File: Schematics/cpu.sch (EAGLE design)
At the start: 42 parts, among them IC10 74LS32N, IC2 LM555N, IC3 LM555N, IC4 7400N, IC5 74LS32N, IC6 74LS32N, IC7 74LS32N, IC8 74154N, IC9 74154N, U1 74HC245N,652, U10 74HC373N,652, U11 74HC373N,652, U12 74HC373N,652, U13 74HC373N,652, U14 74HC373N,652, U15 74HC373N,652, U2 74HC245N,652, U3 74HC245N,652, U4 74HC04N,652, U5 74HC373N,652, U6 74HC373N,652, U7 74HC373N,652, U8 74HC373N,652, U9 74HC373N,652

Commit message: started on video board
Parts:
- added U$5: DB15, SparkFun-Connectors:DB15
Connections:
- new net BLUE: U$5.3
- new net GREEN: U$5.2
- new net HSYNC: U$5.13
- new net RED: U$5.1
- new net VSYNC: U$5.14
- net GND: now also U$5.10, U$5.5, U$5.6, U$5.7, U$5.8, U$5.9
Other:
- note added: "Note: Medium speed SRAM is needed 25MHz => 40ns 12.5MHz => 80ns IDT71256SA AS6C62256 SST39SF040"
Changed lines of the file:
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@@
 <part name="GND26" library="SparkFun-Aesthetics" deviceset="GND" device=""/>
 <part name="SUPPLY11" library="SparkFun-Aesthetics" deviceset="VCC" device="" value="+5V"/>
+<part name="U$5" library="SparkFun-Connectors" deviceset="DB15" device=""/>
+<part name="GND27" library="supply1" deviceset="GND" device=""/>
 </parts>
 <sheets>
@@
 </segment>
 </net>
+</nets>
+</sheet>
+<sheet>
+<description>VGA Video Generator</description>
+<plain>
+<text x="10.16" y="30.48" size="1.778" layer="97">Note:
+Medium speed SRAM is needed
+25MHz =&gt; 40ns
+12.5MHz =&gt; 80ns
+IDT71256SA
+AS6C62256
+SST39SF040</text>
+</plain>
+<instances>
+<instance part="U$5" gate="G$1" x="53.34" y="-2.54"/>
+<instance part="GND27" gate="1" x="40.64" y="-30.48"/>
+</instances>
+<busses>
+</busses>
+<nets>
+<net name="RED" class="0">
+<segment>
+<pinref part="U$5" gate="G$1" pin="1"/>
+<wire x1="45.72" y1="5.08" x2="33.02" y2="5.08" width="0.1524" layer="91"/>
+<label x="35.56" y="5.08" size="1.778" layer="95"/>
+</segment>
+</net>
+<net name="GREEN" class="0">
+<segment>
+<pinref part="U$5" gate="G$1" pin="2"/>
+<wire x1="45.72" y1="0" x2="33.02" y2="0" width="0.1524" layer="91"/>
+<label x="35.56" y="0" size="1.778" layer="95"/>
+</segment>
+</net>
+<net name="BLUE" class="0">
+<segment>
+<pinref part="U$5" gate="G$1" pin="3"/>
+<wire x1="45.72" y1="-5.08" x2="33.02" y2="-5.08" width="0.1524" layer="91"/>
+<label x="35.56" y="-5.08" size="1.778" layer="95"/>
+</segment>
+</net>
+<net name="HSYNC" class="0">
+<segment>
+<pinref part="U$5" gate="G$1" pin="13"/>
+<wire x1="61.214" y1="-5.08" x2="73.66" y2="-5.08" width="0.1524" layer="91"/>
+<label x="68.58" y="-5.08" size="1.778" layer="95"/>
+</segment>
+</net>
+<net name="VSYNC" class="0">
+<segment>
+<pinref part="U$5" gate="G$1" pin="14"/>
+<wire x1="61.214" y1="-10.16" x2="73.66" y2="-10.16" width="0.1524" layer="91"/>
+<label x="68.58" y="-10.16" size="1.778" layer="95"/>
+</segment>
+</net>
+<net name="GND" class="0">
+<segment>
+<pinref part="U$5" gate="G$1" pin="6"/>
+<wire x1="61.214" y1="7.62" x2="63.5" y2="7.62" width="0.1524" layer="91"/>
+<wire x1="63.5" y1="7.62" x2="63.5" y2="2.54" width="0.1524" layer="91"/>
+<wire x1="63.5" y1="2.54" x2="63.5" y2="-2.54" width="0.1524" layer="91"/>
+<wire x1="63.5" y1="-2.54" x2="63.5" y2="-7.62" width="0.1524" layer="91"/>
+<wire x1="63.5" y1="-7.62" x2="63.5" y2="-12.7" width="0.1524" layer="91"/>
+<pinref part="U$5" gate="G$1" pin="10"/>
+<wire x1="61.214" y1="-12.7" x2="63.5" y2="-12.7" width="0.1524" layer="91"/>
+<junction x="63.5" y="-12.7"/>
+<pinref part="U$5" gate="G$1" pin="9"/>
+<wire x1="61.214" y1="-7.62" x2="63.5" y2="-7.62" width="0.1524" layer="91"/>
+<junction x="63.5" y="-7.62"/>
+<pinref part="U$5" gate="G$1" pin="8"/>
+<wire x1="61.214" y1="-2.54" x2="63.5" y2="-2.54" width="0.1524" layer="91"/>
+<junction x="63.5" y="-2.54"/>
+<pinref part="U$5" gate="G$1" pin="7"/>
+<wire x1="61.214" y1="2.54" x2="63.5" y2="2.54" width="0.1524" layer="91"/>
+<junction x="63.5" y="2.54"/>
+<wire x1="63.5" y1="-12.7" x2="63.5" y2="-22.86" width="0.1524" layer="91"/>
+<pinref part="U$5" gate="G$1" pin="5"/>
+<wire x1="45.72" y1="-15.24" x2="40.64" y2="-15.24" width="0.1524" layer="91"/>
+<wire x1="40.64" y1="-15.24" x2="40.64" y2="-22.86" width="0.1524" layer="91"/>
+<wire x1="63.5" y1="-22.86" x2="40.64" y2="-22.86" width="0.1524" layer="91"/>
+<wire x1="40.64" y1="-22.86" x2="40.64" y2="-27.94" width="0.1524" layer="91"/>
+<junction x="40.64" y="-22.86"/>
+<pinref part="GND27" gate="1" pin="GND"/>
+</segment>
+</net>

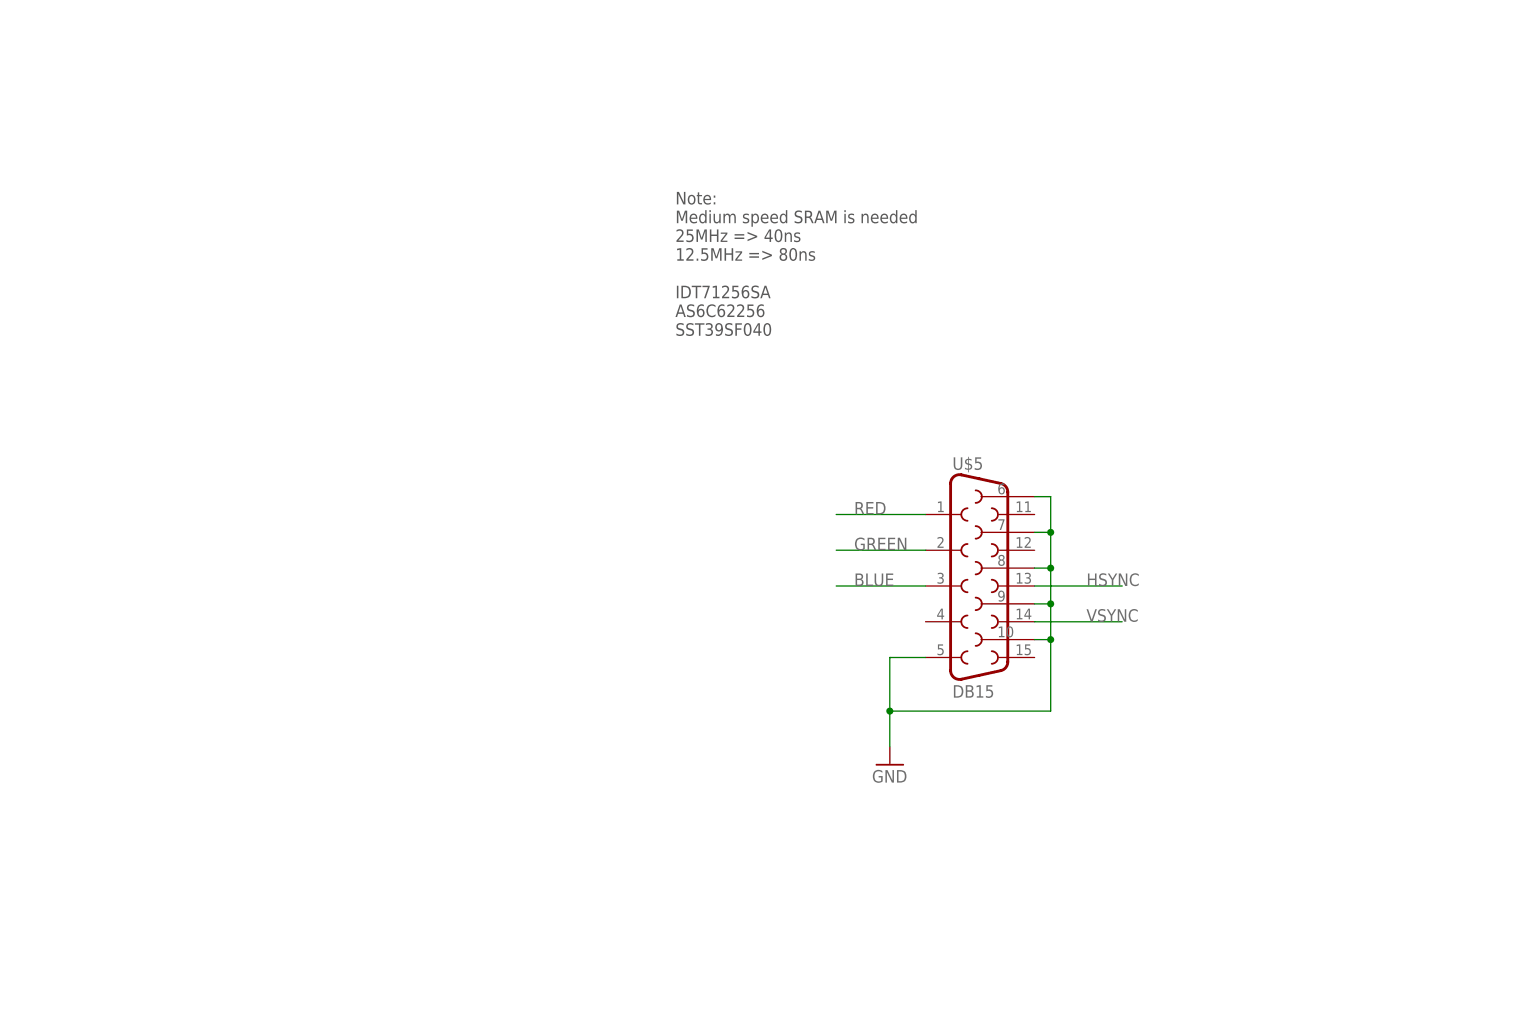
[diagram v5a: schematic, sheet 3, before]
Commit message: created resistor ladder
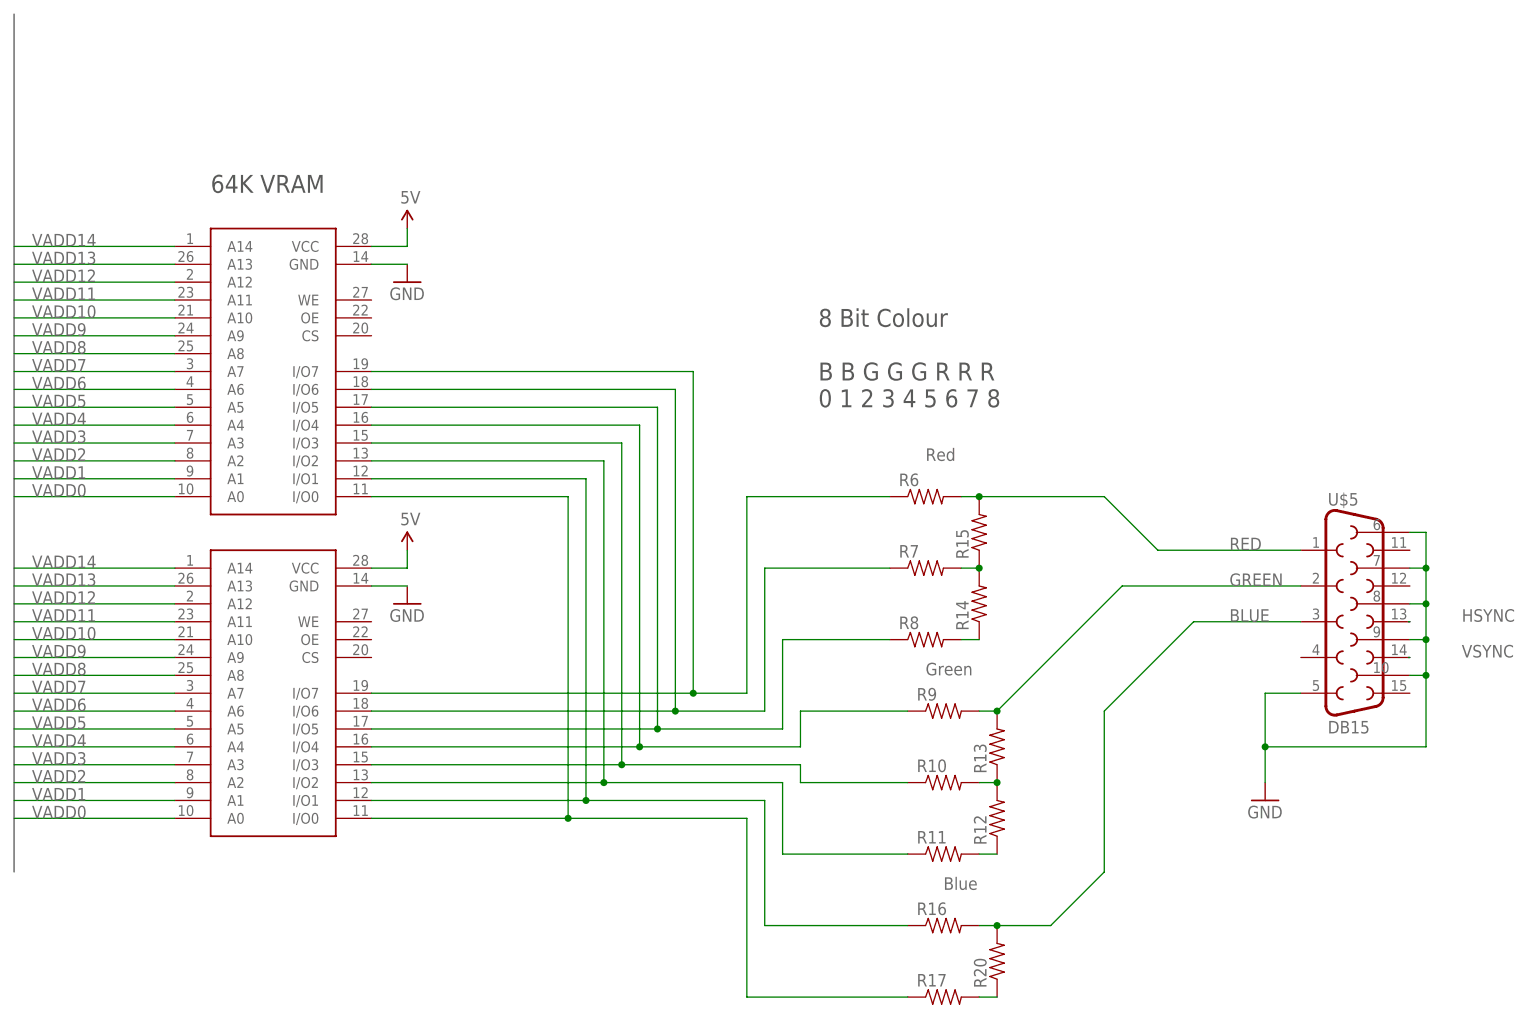
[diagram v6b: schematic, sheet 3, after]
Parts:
- added R10, R11, R12, R13, R14, R15, R16, R17, R20, R6, R7, R8, R9: (no value), SparkFun-Resistors:RESISTORPTH-1/4W
- added U$6, U$7: IDT71256SA, JacobBooth:IDT71256SA
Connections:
- new net N$41: R17.1, U$6.I/O0, U$7.I/O0
- new net N$42: R16.1, U$6.I/O1, U$7.I/O1
- new net N$43: R11.1, U$6.I/O2, U$7.I/O2
- new net N$44: R10.1, U$6.I/O3, U$7.I/O3
- new net N$45: R9.1, U$6.I/O4, U$7.I/O4
- new net N$46: R8.1, U$6.I/O5, U$7.I/O5
- new net N$47: R7.1, U$6.I/O6, U$7.I/O6
- new net N$48: R6.1, U$6.I/O7, U$7.I/O7
- new net N$49: R14.1, R8.2
- new net N$52: R14.2, R15.1, R7.2
- new net N$56: R11.2, R12.1
- new net N$57: R10.2, R12.2, R13.1
- new net N$62: R17.2, R20.1
- new net VADD0: U$6.A0, U$7.A0
- new net VADD1: U$6.A1, U$7.A1
- new net VADD10: U$6.A10, U$7.A10
- new net VADD11: U$6.A11, U$7.A11
- new net VADD12: U$6.A12, U$7.A12
- new net VADD13: U$6.A13, U$7.A13
- new net VADD14: U$6.A14, U$7.A14
- new net VADD2: U$6.A2, U$7.A2
- new net VADD3: U$6.A3, U$7.A3
- new net VADD4: U$6.A4, U$7.A4
- new net VADD5: U$6.A5, U$7.A5
- new net VADD6: U$6.A6, U$7.A6
- new net VADD7: U$6.A7, U$7.A7
- new net VADD8: U$6.A8, U$7.A8
- new net VADD9: U$6.A9, U$7.A9
- net 5V: now also U$6.VCC, U$7.VCC
- net BLUE: now also R16.2, R20.2
- net GND: now also U$6.GND, U$7.GND
- net GREEN: now also R13.2, R9.2
- net RED: now also R15.2, R6.2
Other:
- note added: "64K VRAM"
- note added: "8 Bit Colour B B G G G R R R 0 1 2 3 4 5 6 7 8"
- note added: "Blue"
- note added: "Green"
- note added: "Red"
- note removed: "Note: Medium speed SRAM is needed 25MHz => 40ns 12.5MHz => 80ns IDT71256SA AS6C62256 SST39SF040"
- moved on the sheet: U$5
